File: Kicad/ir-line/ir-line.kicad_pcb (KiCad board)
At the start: 2 copper layers, 74 x 20 mm, 30 parts, among them IC1 VISHAY-CNY70, IC2 VISHAY-CNY70, IC3 VISHAY-CNY70, IC4 VISHAY-CNY70, IC5 VISHAY-CNY70, IC6 TPS92612, IC7 TPS92612, K1 FRONT #1, K2 FRONT #2

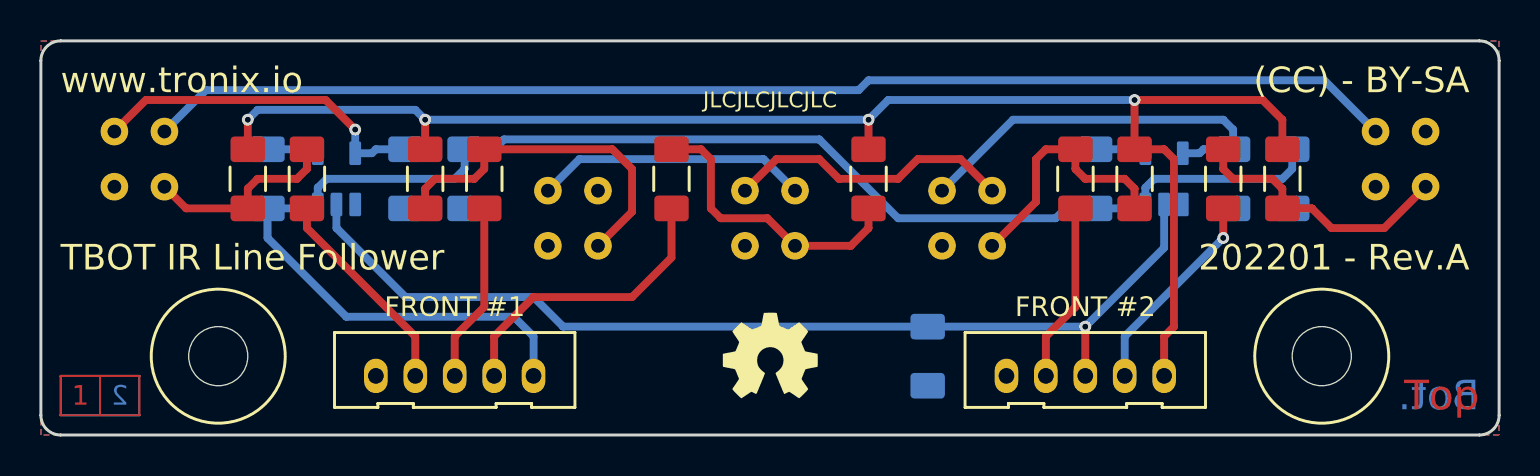
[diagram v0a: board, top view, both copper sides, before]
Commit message: Update IR-LINE
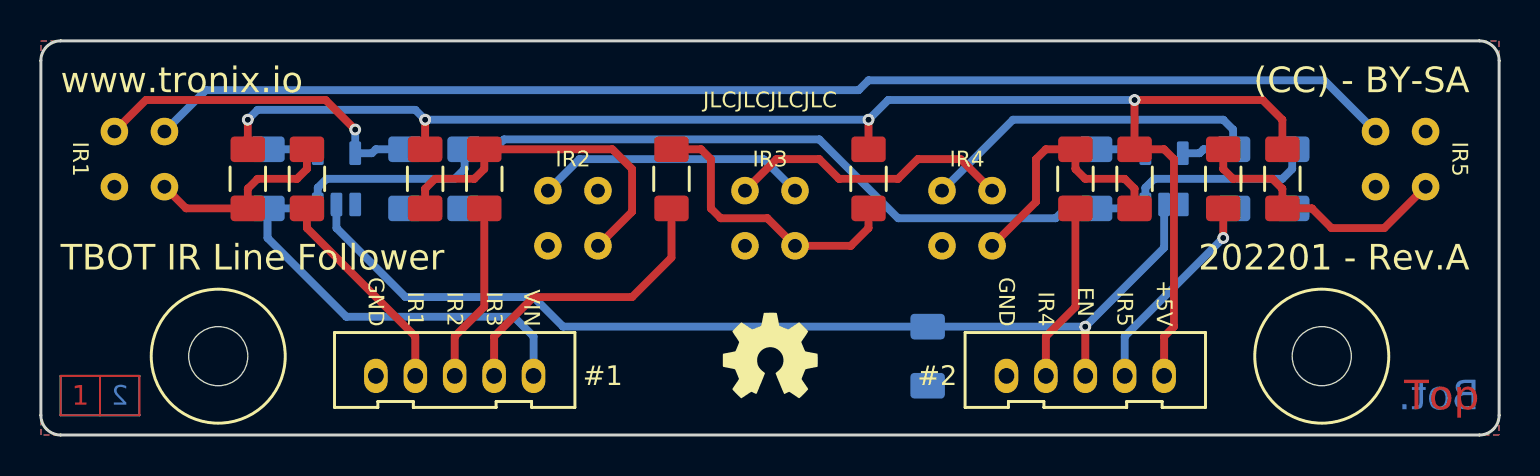
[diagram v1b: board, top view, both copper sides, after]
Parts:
- K1, K2: footprint tronixio:zzMOLEX-532530570 -> tronixio:MOLEX-532530570
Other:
- board text added: "#1"
- board text added: "#2"
- board text added: "+5V"
- board text added: "EN"
- board text added: "GND"
- board text added: "IR1"
- board text added: "IR2"
- board text added: "IR3"
- board text added: "IR4"
- board text added: "IR5"
- board text added: "VIN"
- board text removed: "FRONT #1"
- board text removed: "FRONT #2"

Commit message: Update IR-LINE
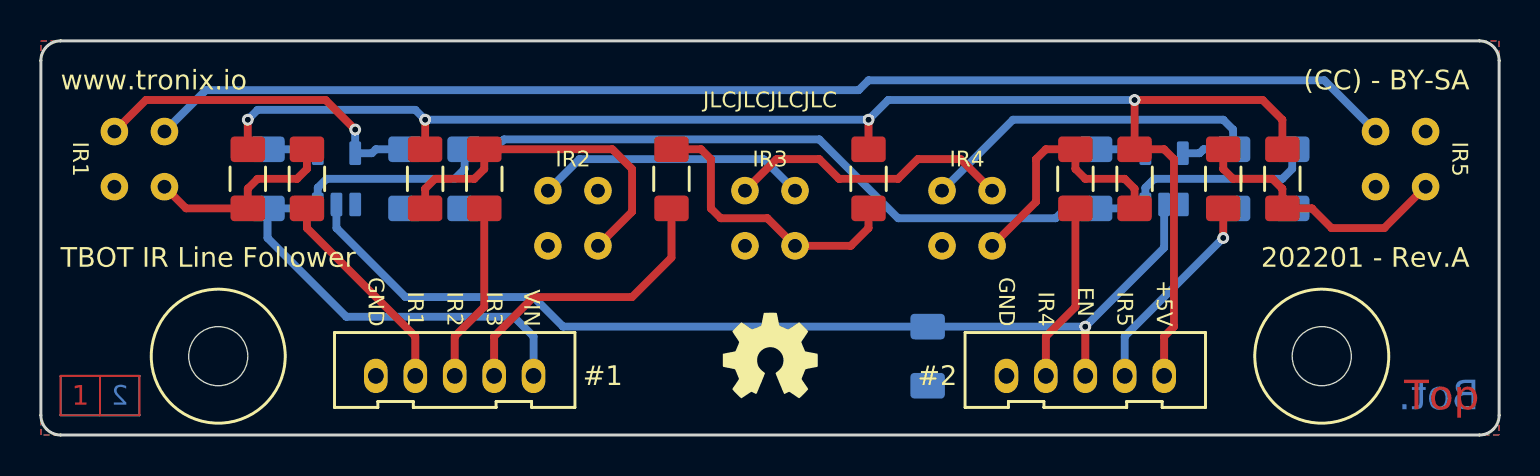
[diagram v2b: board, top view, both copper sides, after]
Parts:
- IC1, IC2, IC3, IC4, IC5: footprint tronixio:zzVISHAY-CNY70 -> tronixio:VISHAY-CNY70
